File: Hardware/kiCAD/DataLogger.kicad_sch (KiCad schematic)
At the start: 38 parts, among them J1 On/Off, J10 Conn_01x02_Pin, J2 RTC_Batt, J3 Uart1, J5 Mounting Hole, J6 Mounting Hole, J7 Mounting Hole, J8 Mounting Hole, Q1 2N7002, Q2 2N7002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

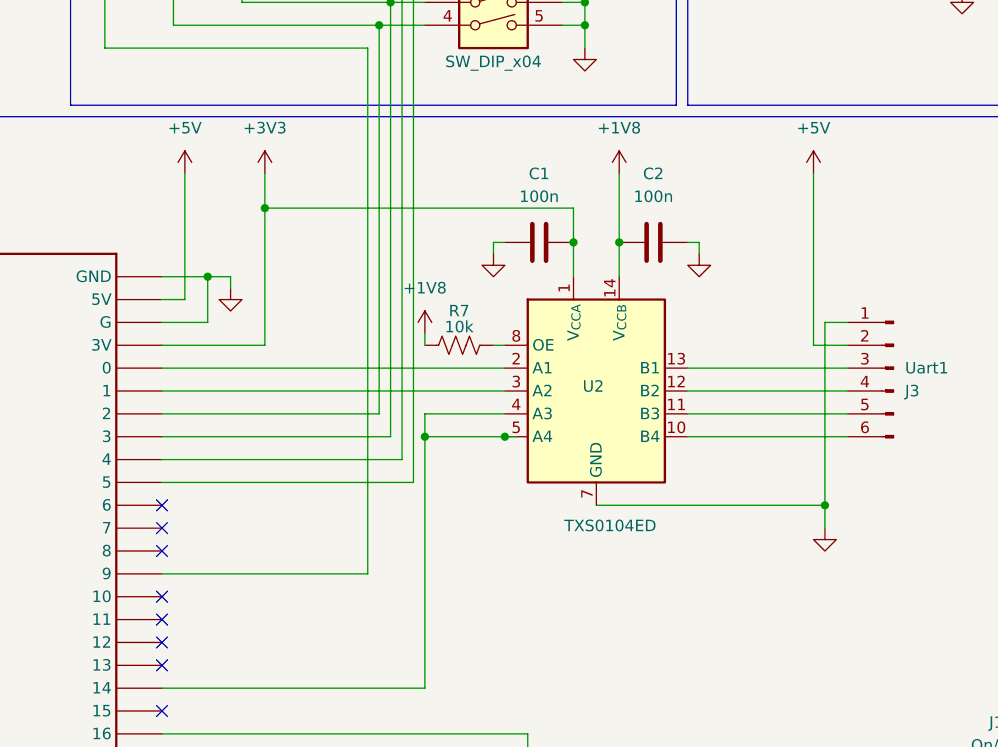
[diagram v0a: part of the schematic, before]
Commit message: TXS0104ED wiring fix and layout adjustments for improved SD card access. REV2.1
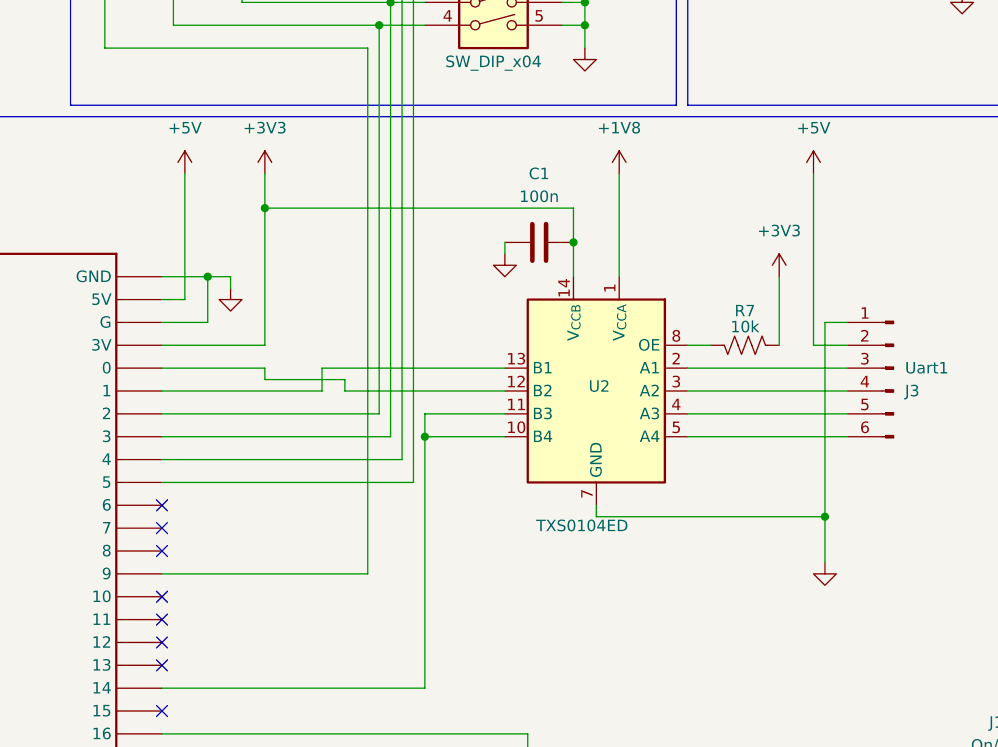
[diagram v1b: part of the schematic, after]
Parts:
- removed C2: 100n, Capacitor_SMD:C_0805_2012Metric_Pad1.18x1.45mm_HandSolder, symbol Device:C
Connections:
- net +1V8: now also U2.1 (V_{CCA}); no longer R7.1, U2.14 (V_{CCB})
- net +3V3: now also R7.1, U2.14 (V_{CCB}); no longer U2.1 (V_{CCA})
- net at J3.3 (Pin_3): now also U2.2 (A1); no longer U2.13 (B1)
- net at J3.4 (Pin_4): now also U2.3 (A2); no longer U2.12 (B2)
- net at J3.5 (Pin_5): now also U2.4 (A3); no longer U2.11 (B3)
- net at J3.6 (Pin_6): now also U2.5 (A4); no longer U2.10 (B4)
- net at T1.0: now also U2.12 (B2); no longer U2.2 (A1)
- net at T1.1: now also U2.13 (B1); no longer U2.3 (A2)
- new net: T1.14, U2.10 (B4), U2.11 (B3)
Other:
- moved on the sheet: R7
